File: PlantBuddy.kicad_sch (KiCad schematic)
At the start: 66 parts, among them J1 USB_C_Receptacle_USB2.0, J101 JST, J102 J-Link SWD, J4 External, Q101 DMG1012T, SW1 SW_Push, U1 LTR-303ALS-01, U101 RT9080-33GJ5, U102 nRF52832-QFxx, U104 XB5350A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

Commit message: Fixes & ordered.
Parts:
- added TP101: TP_3V3, TestPoint:TestPoint_Pad_D1.0mm, symbol Connector:TestPoint_Small
- added TP102: TP_s3V3, TestPoint:TestPoint_Pad_D1.0mm, symbol Connector:TestPoint_Small
- added TP103: TP_VIN, TestPoint:TestPoint_Pad_D1.0mm, symbol Connector:TestPoint_Small
- added TP104: TP_VIO, TestPoint:TestPoint_Pad_D1.0mm, symbol Connector:TestPoint_Small
- D1: value XL-3528RGBW-WS2812B -> SK6812SMINI-ER; LCSC C2890364 -> C5142047
- L101: LCSC C14033 -> C76775
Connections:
- net +3V3: now also TP101.1
- net SCL: now also U102.11 (NFC1/P0.09); no longer U102.12 (NFC2/P0.10)
- net SDA: now also U102.10 (P0.08); no longer U102.11 (NFC1/P0.09)
- net S_3V3: now also TP102.1
- net VBUS: now also TP103.1
- net V_IO: now reaches R105.2, U106.6 (VDD)
- net V_IO: now also TP104.1
- no-connect marks 21 -> 29
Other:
- note added: "FREQ_OUT"
- note added: "I2C1_SCL"
- note added: "I2C1_SDA"
- note added: "I2C2_SCL"
- note added: "I2C2_SDA"
- note added: "Might not be needed because of the integrated Power On Reset circuit"
- moved on the sheet: R3

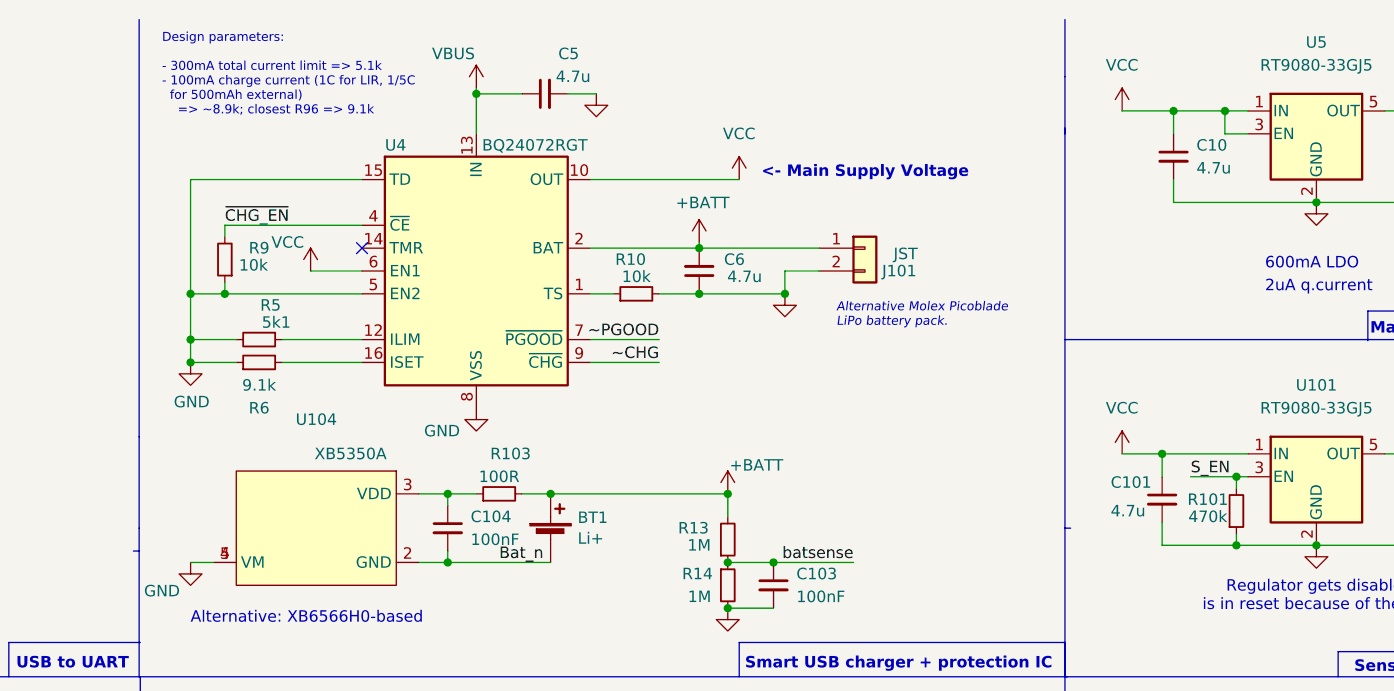
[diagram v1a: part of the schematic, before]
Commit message: Slight BOM consolidation.
- Changed 9.1k resistor to a 10k one.
- Changed 470k resistor to a 1Meg one.
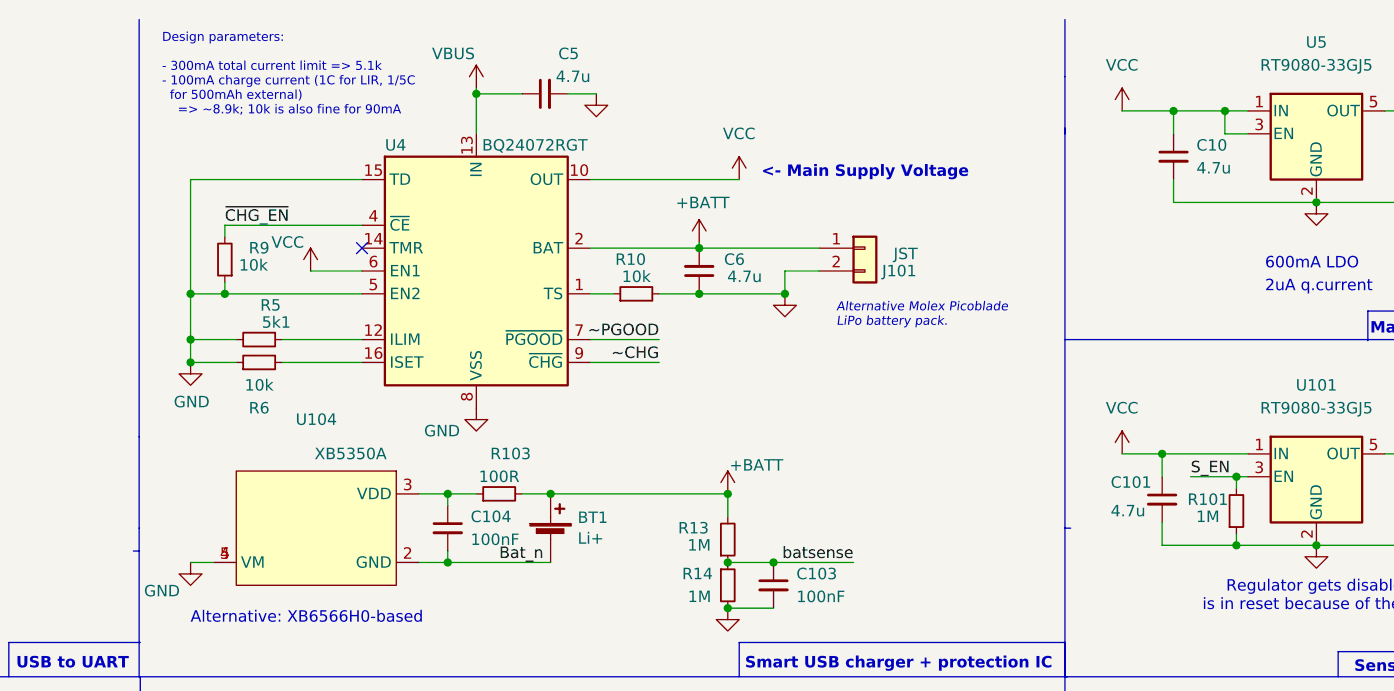
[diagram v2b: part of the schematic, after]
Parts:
- R101: value 470k -> 1M; LCSC C25790 -> C26083
- R6: value 9.1k -> 10k; footprint Resistor_SMD:R_0603_1608Metric -> Resistor_SMD:R_0402_1005Metric; LCSC C23260 -> C25744
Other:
- note added: "Design parameters: - 300mA total current limit => 5.1k - 100mA charge current (1C for LIR, 1/5C for 500mAh external) => ~8.9k; 10k is also fine for 90mA"
- note removed: "Design parameters: - 300mA total current limit => 5.1k - 100mA charge current (1C for LIR, 1/5C for 500mAh external) => ~8.9k; closest R96 => 9.1k"
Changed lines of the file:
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@@
     (effects (font (size 1.27 1.27) bold) (justify right bottom))
   )
-  (text "Design parameters:\n\n- 300mA total current limit => 5.1k\n- 100mA charge current (1C for LIR, 1/5C\n  for 500mAh external) \n    => ~8.9k; closest R96 => 9.1k\n"
+  (text "Design parameters:\n\n- 300mA total current limit => 5.1k\n- 100mA charge current (1C for LIR, 1/5C\n  for 500mAh external) \n    => ~8.9k; 10k is also fine for 90mA\n"
     (at 254.508 22.86 0)
     (effects (font (size 1 1)) (justify left bottom))
@@
     (in_bom yes) (on_board yes)
     (property "Reference" "R101" (id 0) (at 370.713 65.405 0))
-    (property "Value" "470k" (id 1) (at 370.713 67.31 0))
+    (property "Value" "1M" (id 1) (at 370.713 67.31 0))
     (property "Footprint" "Resistor_SMD:R_0402_1005Metric" (id 2) (at 373.888 66.675 0)
       (effects (font (size 1.27 1.27)) hide)
@@
       (effects (font (size 1.27 1.27)) hide)
     )
-    (property "LCSC" "C25790" (id 4) (at 373.888 66.675 90)
+    (property "LCSC" "C26083" (id 4) (at 373.888 66.675 90)
       (effects (font (size 1.27 1.27)) hide)
     )
@@
     (in_bom yes) (on_board yes)
     (property "Reference" "R6" (id 0) (at 265.303 55.245 90))
-    (property "Value" "9.1k" (id 1) (at 265.303 52.705 90))
-    (property "Footprint" "Resistor_SMD:R_0603_1608Metric" (id 2) (at 265.303 50.165 0)
+    (property "Value" "10k" (id 1) (at 265.303 52.705 90))
+    (property "Footprint" "Resistor_SMD:R_0402_1005Metric" (id 2) (at 265.303 50.165 0)
       (effects (font (size 1.27 1.27)) hide)
     )
@@
       (effects (font (size 1.27 1.27)) hide)
     )
-    (property "LCSC" "C23260" (id 4) (at 265.303 50.165 90)
+    (property "LCSC" "C25744" (id 4) (at 265.303 50.165 90)
       (effects (font (size 1.27 1.27)) hide)
     )
@@
     )
     (path "/8668760b-bf0c-46d5-888b-b7a19a113ccc"
-      (reference "R6") (unit 1) (value "9.1k") (footprint "Resistor_SMD:R_0603_1608Metric")
+      (reference "R6") (unit 1) (value "10k") (footprint "Resistor_SMD:R_0402_1005Metric")
     )
     (path "/caee7869-b53b-4a0f-937a-3d9a9ad5dbdb"
@@
     )
     (path "/5c2e072e-eefe-4efb-8ddf-df56fde743a4"
-      (reference "R101") (unit 1) (value "470k") (footprint "Resistor_SMD:R_0402_1005Metric")
+      (reference "R101") (unit 1) (value "1M") (footprint "Resistor_SMD:R_0402_1005Metric")
     )
     (path "/1dd523e6-5c69-4236-9e58-0ab57c68caee"
